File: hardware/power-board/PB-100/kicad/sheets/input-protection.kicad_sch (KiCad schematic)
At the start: 0 parts

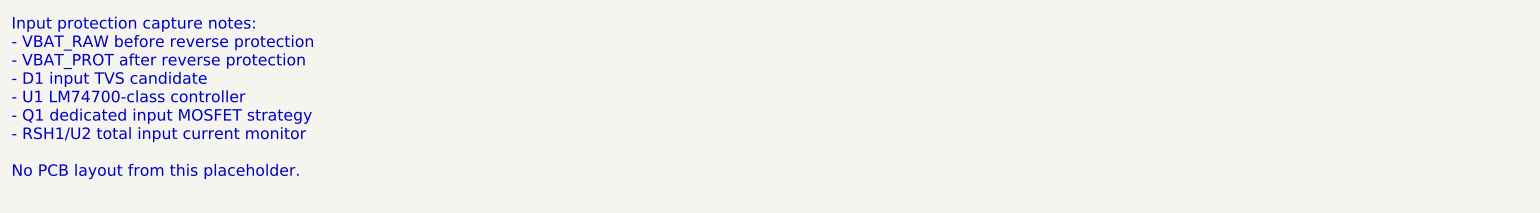
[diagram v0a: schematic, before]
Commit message: hardware: sync pb100 kicad sheet trace notes
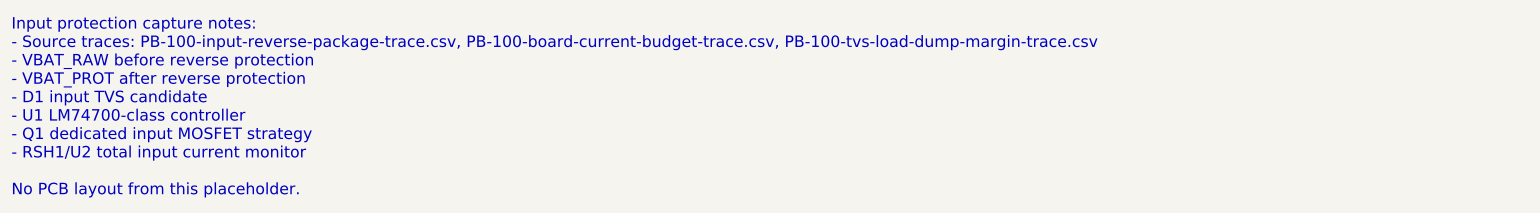
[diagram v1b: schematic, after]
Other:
- note added: "Input protection capture notes: - Source traces: PB-100-input-reverse-package-trace.csv, PB-100-board-current-budget-trace.csv, PB-100-tvs-load-dump-margin-trace.csv - VBAT_RAW before reverse protection - VBAT_PROT after reverse protection - D1 input TVS candidate - U1 LM74700-class controller - Q1 dedicated input MOSFET strategy - RSH1/U2 total input current monitor No PCB layout from this place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"
- note removed: "Input protection capture notes: - VBAT_RAW before reverse protection - VBAT_PROT after reverse protection - D1 input TVS candidate - U1 LM74700-class controller - Q1 dedicated input MOSFET strategy - RSH1/U2 total input current monitor No PCB layout from this placeholder."
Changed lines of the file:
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@@
     (comment 9 "Work queue: CAP-INP. Input protection capture is blocked on Q1 INPUT_REVERSE_FET evidence.")
     (comment 1 "Placeholder sheet. Capture battery input, TVS, reverse protection, input telemetry here.")
-    (comment 2 "Source docs: PB-100-input-reverse-protection.md and PB-100-protection-validation.csv.")
+    (comment 2 "Sources: PB-100-input-reverse-package-trace.csv, PB-100-board-current-budget-trace.csv, PB-100-tvs-load-dump-margin-trace.csv.")
   )
-  (text "Input protection capture notes:\n- VBAT_RAW before reverse protection\n- VBAT_PROT after reverse protection\n- D1 input TVS candidate\n- U1 LM74700-class controller\n- Q1 dedicated input MOSFET strategy\n- RSH1/U2 total input current monitor\n\nNo PCB layout from this placeholder."
+  (text "Input protection capture notes:\n- Source traces: PB-100-input-reverse-package-trace.csv, PB-100-board-current-budget-trace.csv, PB-100-tvs-load-dump-margin-trace.csv\n- VBAT_RAW before reverse protection\n- VBAT_PROT after reverse protection\n- D1 input TVS candidate\n- U1 LM74700-class controller\n- Q1 dedicated input MOSFET strategy\n- RSH1/U2 total input current monitor\n\nNo PCB layout from this placeholder."
     (at 25 30 0)
     (effects (font (size 2.0 2.0)) (justify left top))

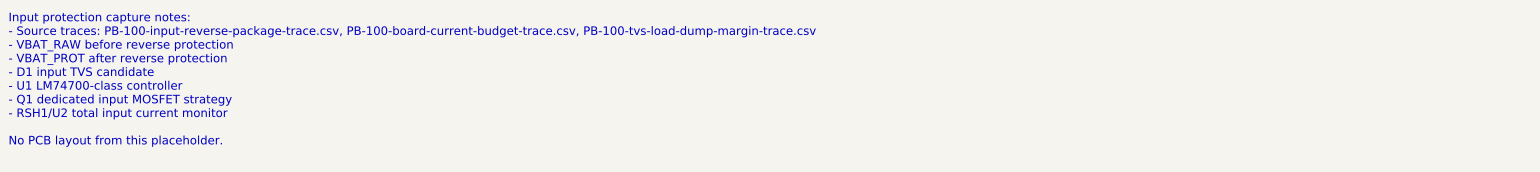
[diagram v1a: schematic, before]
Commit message: hardware: add pb100 40a current budget review
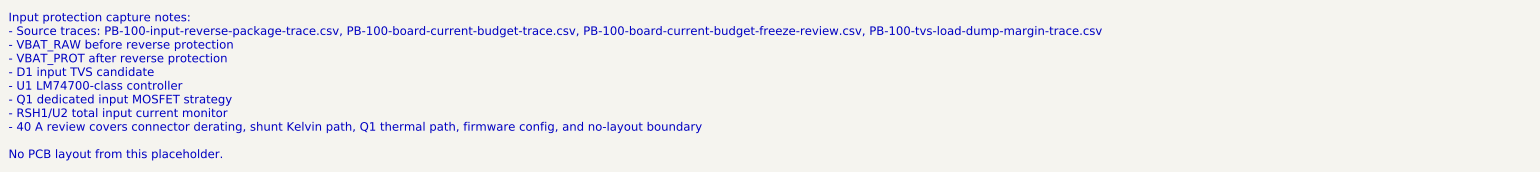
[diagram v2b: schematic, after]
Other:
- note added: "Input protection capture notes: - Source traces: PB-100-input-reverse-package-trace.csv, PB-100-board-current-budget-trace.csv, PB-100-board-current-budget-freeze-review.csv, PB-100-tvs-load-dump-margin-trace.csv - VBAT_RAW before reverse protection - VBAT_PROT after reverse protection - D1 input TVS candidate - U1 LM74700-class controller - Q1 dedicated input MOSFET strategy - RSH1/U2 total inpu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"
- note removed: "Input protection capture notes: - Source traces: PB-100-input-reverse-package-trace.csv, PB-100-board-current-budget-trace.csv, PB-100-tvs-load-dump-margin-trace.csv - VBAT_RAW before reverse protection - VBAT_PROT after reverse protection - D1 input TVS candidate - U1 LM74700-class controller - Q1 dedicated input MOSFET strategy - RSH1/U2 total input current monitor No PCB layout from this place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"
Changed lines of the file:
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@@
     (comment 9 "Work queue: CAP-INP. Input protection capture is blocked on Q1 INPUT_REVERSE_FET evidence.")
     (comment 1 "Placeholder sheet. Capture battery input, TVS, reverse protection, input telemetry here.")
-    (comment 2 "Sources: PB-100-input-reverse-package-trace.csv, PB-100-board-current-budget-trace.csv, PB-100-tvs-load-dump-margin-trace.csv.")
+    (comment 2 "Sources: PB-100-input-reverse-package-trace.csv, PB-100-board-current-budget-trace.csv, PB-100-board-current-budget-freeze-review.csv, PB-100-tvs-load-dump-margin-trace.csv.")
   )
-  (text "Input protection capture notes:\n- Source traces: PB-100-input-reverse-package-trace.csv, PB-100-board-current-budget-trace.csv, PB-100-tvs-load-dump-margin-trace.csv\n- VBAT_RAW before reverse protection\n- VBAT_PROT after reverse protection\n- D1 input TVS candidate\n- U1 LM74700-class controller\n- Q1 dedicated input MOSFET strategy\n- RSH1/U2 total input current monitor\n\nNo PCB layout from this placeholder."
+  (text "Input protection capture notes:\n- Source traces: PB-100-input-reverse-package-trace.csv, PB-100-board-current-budget-trace.csv, PB-100-board-current-budget-freeze-review.csv, PB-100-tvs-load-dump-margin-trace.csv\n- VBAT_RAW before reverse protection\n- VBAT_PROT after reverse protection\n- D1 input TVS candidate\n- U1 LM74700-class controller\n- Q1 dedicated input MOSFET strategy\n- RSH1/U2 total input current monitor\n- 40 A review covers connector derating, shunt Kelvin path, Q1 thermal path, firmware config, and no-layout boundary\n\nNo PCB layout from this placeholder."
     (at 25 30 0)
     (effects (font (size 2.0 2.0)) (justify left top))

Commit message: hardware: add pb100 input reverse freeze review
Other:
- note added: "Input protection capture notes: - Source traces: PB-100-input-reverse-package-trace.csv, PB-100-input-reverse-freeze-review.csv, PB-100-board-current-budget-trace.csv, PB-100-board-current-budget-freeze-review.csv, PB-100-tvs-load-dump-margin-trace.csv - VBAT_RAW before reverse protection - VBAT_PROT after reverse protection - D1 input TVS candidate - U1 LM74700-class controller - Q1 dedicated in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"
- note removed: "Input protection capture notes: - Source traces: PB-100-input-reverse-package-trace.csv, PB-100-board-current-budget-trace.csv, PB-100-board-current-budget-freeze-review.csv, PB-100-tvs-load-dump-margin-trace.csv - VBAT_RAW before reverse protection - VBAT_PROT after reverse protection - D1 input TVS candidate - U1 LM74700-class controller - Q1 dedicated input MOSFET strategy - RSH1/U2 total inpu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"
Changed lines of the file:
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@@
     (comment 9 "Work queue: CAP-INP. Input protection capture is blocked on Q1 INPUT_REVERSE_FET evidence.")
     (comment 1 "Placeholder sheet. Capture battery input, TVS, reverse protection, input telemetry here.")
-    (comment 2 "Sources: PB-100-input-reverse-package-trace.csv, PB-100-board-current-budget-trace.csv, PB-100-board-current-budget-freeze-review.csv, PB-100-tvs-load-dump-margin-trace.csv.")
+    (comment 2 "Sources: PB-100-input-reverse-package-trace.csv, PB-100-input-reverse-freeze-review.csv, PB-100-board-current-budget-trace.csv, PB-100-board-current-budget-freeze-review.csv, PB-100-tvs-load-dump-margin-trace.csv.")
   )
-  (text "Input protection capture notes:\n- Source traces: PB-100-input-reverse-package-trace.csv, PB-100-board-current-budget-trace.csv, PB-100-board-current-budget-freeze-review.csv, PB-100-tvs-load-dump-margin-trace.csv\n- VBAT_RAW before reverse protection\n- VBAT_PROT after reverse protection\n- D1 input TVS candidate\n- U1 LM74700-class controller\n- Q1 dedicated input MOSFET strategy\n- RSH1/U2 total input current monitor\n- 40 A review covers connector derating, shunt Kelvin path, Q1 thermal path, firmware config, and no-layout boundary\n\nNo PCB layout from this placeholder."
+  (text "Input protection capture notes:\n- Source traces: PB-100-input-reverse-package-trace.csv, PB-100-input-reverse-freeze-review.csv, PB-100-board-current-budget-trace.csv, PB-100-board-current-budget-freeze-review.csv, PB-100-tvs-load-dump-margin-trace.csv\n- VBAT_RAW before reverse protection\n- VBAT_PROT after reverse protection\n- D1 input TVS candidate\n- U1 LM74700-class controller\n- Q1 dedicated input MOSFET strategy\n- RSH1/U2 total input current monitor\n- 40 A review covers connector derating, shunt Kelvin path, Q1 thermal path, firmware config, and no-layout boundary\n\nNo PCB layout from this placeholder."
     (at 25 30 0)
     (effects (font (size 2.0 2.0)) (justify left top))
